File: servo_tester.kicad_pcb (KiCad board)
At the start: 2 copper layers, 50 x 100 mm, 39 parts, among them IC1 ATTINY2313-S, P1 CONN_01X02, P2 CONN_01X02, Q1 BC847, Q2 BC847, Q3 BC847, Q4 BC847, SW1 SW_PUSH, U1 LM2596

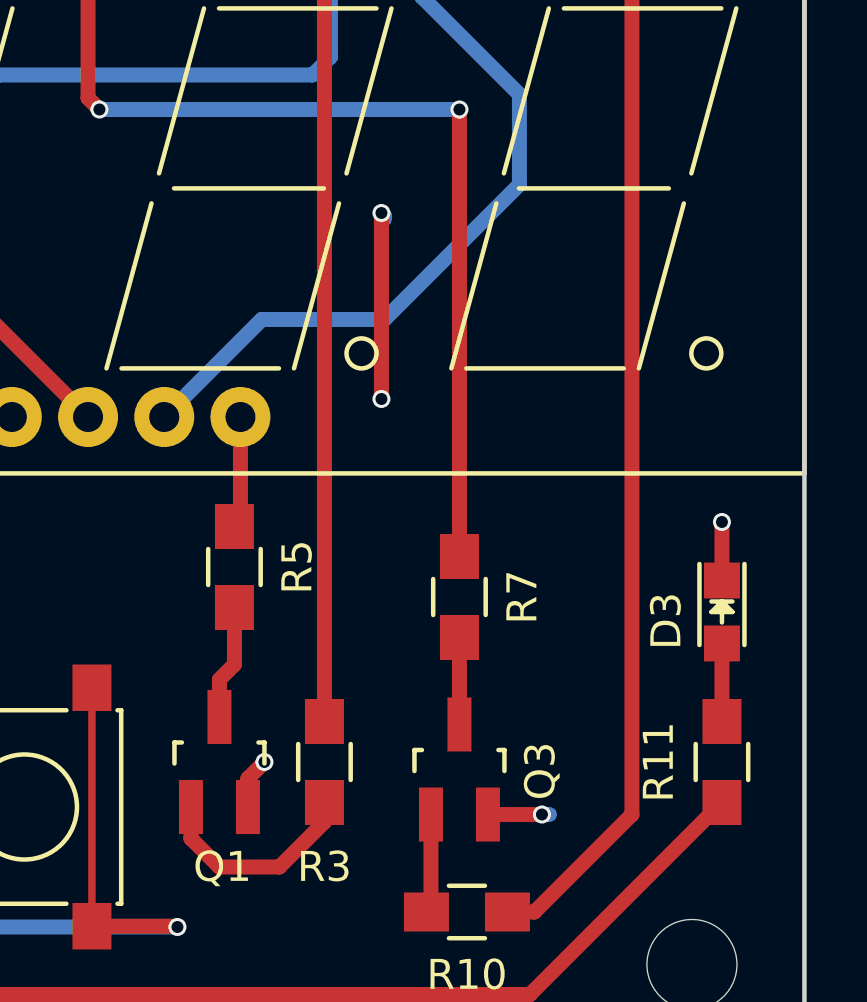
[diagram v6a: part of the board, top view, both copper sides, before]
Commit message: ground connection fix, pcb still neds new netlist
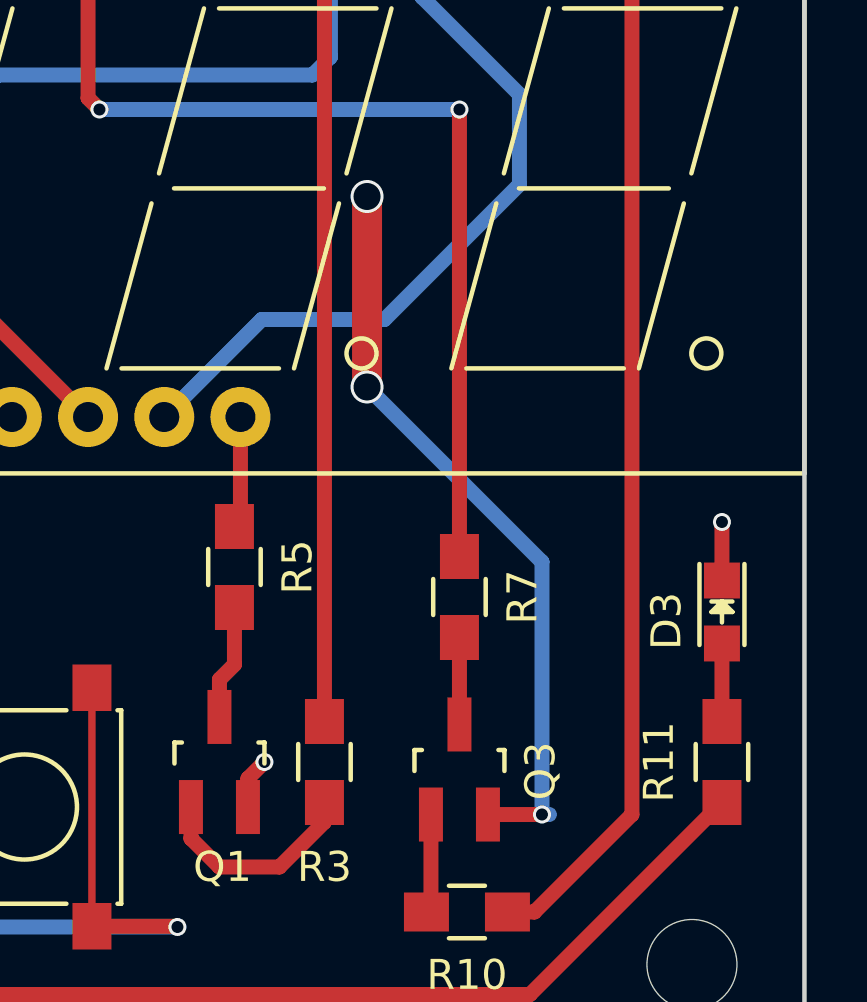
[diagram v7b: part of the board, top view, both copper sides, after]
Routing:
- net GND: track 56.4 -> 80.7 mm, vias 8 -> 10
- net (no net): track 6.81 -> 0.37 mm, vias 2 -> 0
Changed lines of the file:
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@@
-(kicad_pcb (version 4) (host pcbnew 4.0.2+dfsg1-2~bpo8+1-stable)
+(kicad_pcb (version 4) (host pcbnew 4.0.2-stable)
   (general
     (links 77)
@@
     (thickness 1.6)
     (drawings 7)
-    (tracks 332)
+    (tracks 333)
     (zones 0)
     (modules 39)
@@
   (page A4)
   (layers
-    (0 F.Cu signal hide)
-    (31 B.Cu signal hide)
+    (0 F.Cu signal)
+    (31 B.Cu signal)
     (32 B.Adhes user)
     (33 F.Adhes user)
@@
   (gr_line (start 150 50) (end 200 50) (angle 90) (layer Edge.Cuts) (width 0.15))
   (gr_line (start 150 150) (end 150 50) (angle 90) (layer Edge.Cuts) (width 0.15))
-  (segment (start 186 121.4) (end 186 121.3) (width 0.5) (layer B.Cu) (net 0))
-  (via (at 185.9 127.4) (size 0.6) (drill 0.4) (layers F.Cu B.Cu) (net 0))
-  (segment (start 185.9 121.2) (end 185.9 127.4) (width 0.5) (layer F.Cu) (net 0))
-  (via (at 185.9 121.2) (size 0.6) (drill 0.4) (layers F.Cu B.Cu) (net 0))
-  (segment (start 186 121.3) (end 185.9 121.2) (width 0.5) (layer B.Cu) (net 0))
   (segment (start 180.54 65.5) (end 180.5 65.5) (width 0.5) (layer B.Cu) (net 0))
   (segment (start 180.77 65.73) (end 180.54 65.5) (width 0.5) (layer B.Cu) (net 0))
@@
   (segment (start 177.5 95.25) (end 177.5 102.75) (width 0.5) (layer F.Cu) (net 12))
   (segment (start 176.695 94.445) (end 177.5 95.25) (width 0.5) (layer F.Cu) (net 12))
+  (segment (start 185.42 120.65) (end 185.42 121.92) (width 0.5) (layer B.Cu) (net 13))
+  (segment (start 185.42 127) (end 185.42 120.65) (width 1) (layer F.Cu) (net 13))
+  (via (at 185.42 120.65) (size 1.1) (drill 0.9) (layers F.Cu B.Cu) (net 13))
+  (segment (start 191.25 141.25) (end 191.25 132.83) (width 0.5) (layer B.Cu) (net 13))
+  (segment (start 191.25 132.83) (end 185.42 127) (width 0.5) (layer B.Cu) (net 13))
+  (via (at 185.42 127) (size 1.1) (drill 0.9) (layers F.Cu B.Cu) (net 13))
   (segment (start 186.6 67.6) (end 186.6 56.6) (width 0.5) (layer F.Cu) (net 13))
   (segment (start 186.6 56.6) (end 186.5 56.5) (width 0.5) (layer F.Cu) (net 13))
